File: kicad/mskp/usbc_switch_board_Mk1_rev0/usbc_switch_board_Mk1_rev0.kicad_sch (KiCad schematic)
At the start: 26 parts, among them J1 USB_C_Receptacle_USB2.0_14P, J2 USB_C_Receptacle_USB2.0_14P, J3 USB_A, J4 Conn_01x04_Socket, J5 Conn_01x02_Socket, Q1 2N3904, Q2 2N3906, U1 FSUSB42MUX, U2 AMS1117-3.3, U3 AMS1117-2.5

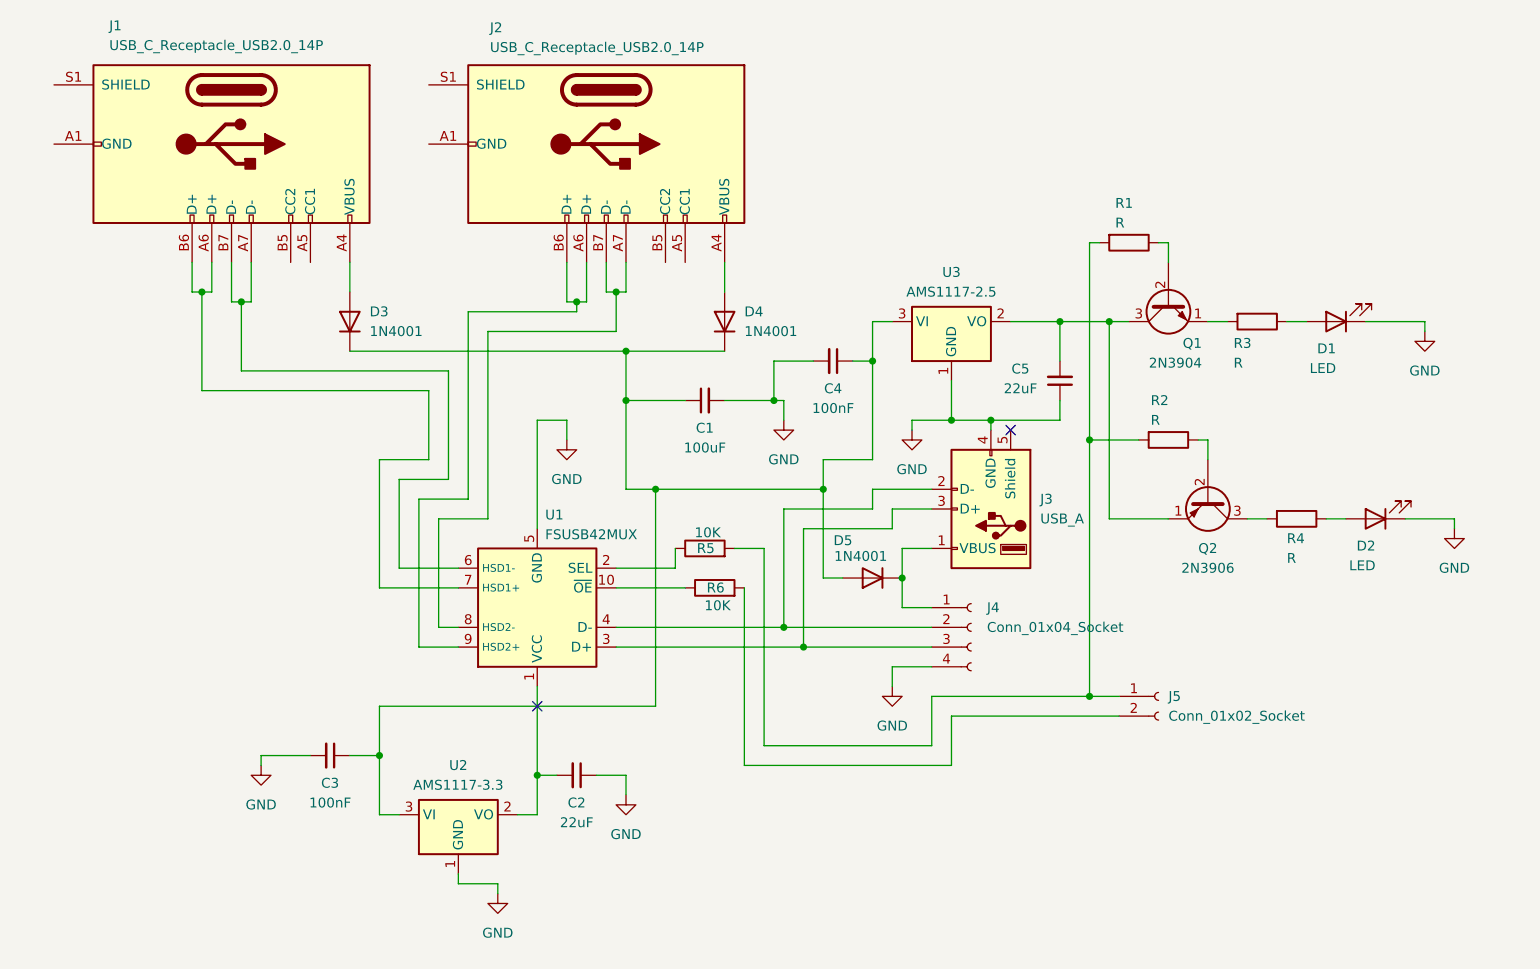
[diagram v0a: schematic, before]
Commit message: Remove unused ctrl mk1r1 in favor of mk2 first draft schematic
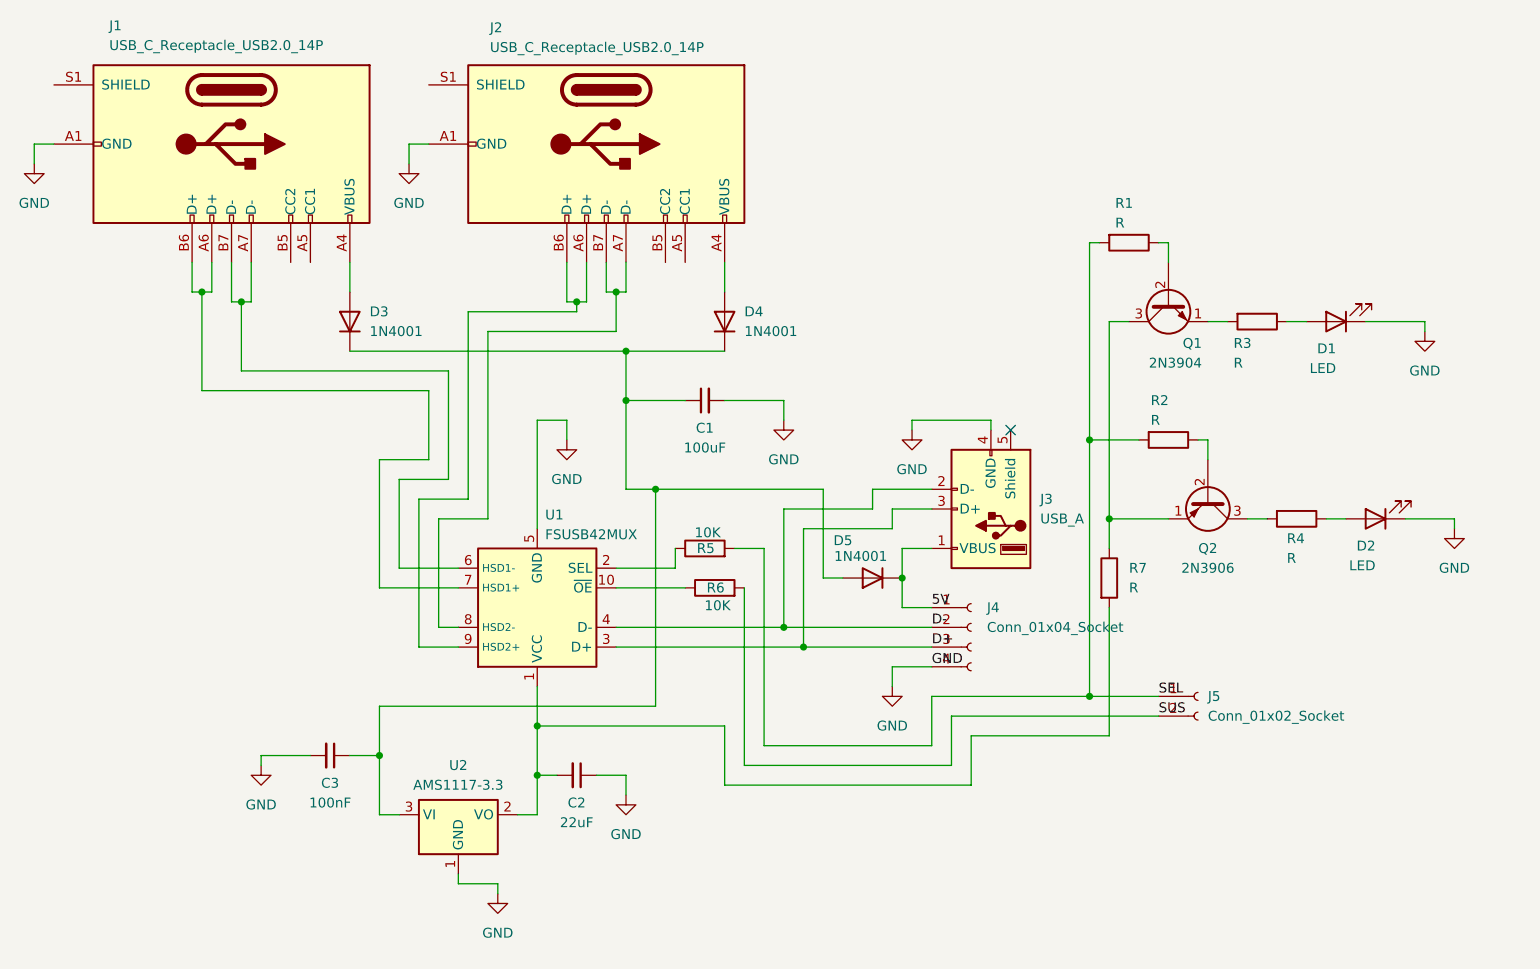
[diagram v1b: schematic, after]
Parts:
- removed C4: 100nF, symbol Device:C_Small
- removed C5: 22uF, symbol Device:C_Small
- removed U3: AMS1117-2.5, Package_TO_SOT_SMD:SOT-223-3_TabPin2, symbol Regulator_Linear:AMS1117-2.5
- added R7: R, symbol Device:R
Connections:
- net GND: now also J1.A1 (GND), J1.A12 (GND), J1.B1 (GND), J1.B12 (GND), J2.A1 (GND), J2.A12 (GND), J2.B1 (GND), J2.B12 (GND)
- net SEL: now reaches J5.1 (Pin_1), R1.2, R2.2, R5.2
- net SUS: now reaches J5.2 (Pin_2), R6.2
- net at C2.2, U1.1 (VCC), U2.2 (VO): now also R7.2
- net D+: now reaches J3.3 (D+), J4.3 (Pin_3), U1.3 (D+)
- net D-: now reaches J3.2 (D-), J4.2 (Pin_2), U1.4 (D-)
- net at Q1.3 (C), Q2.1 (E): now also R7.1
- net 5V: now reaches D5.1 (K), J3.1 (VBUS), J4.1 (Pin_1)
- no-connect marks 2 -> 1
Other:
- moved on the sheet: J5

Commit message: Adds first drafts of adc mouse and io expander mk2
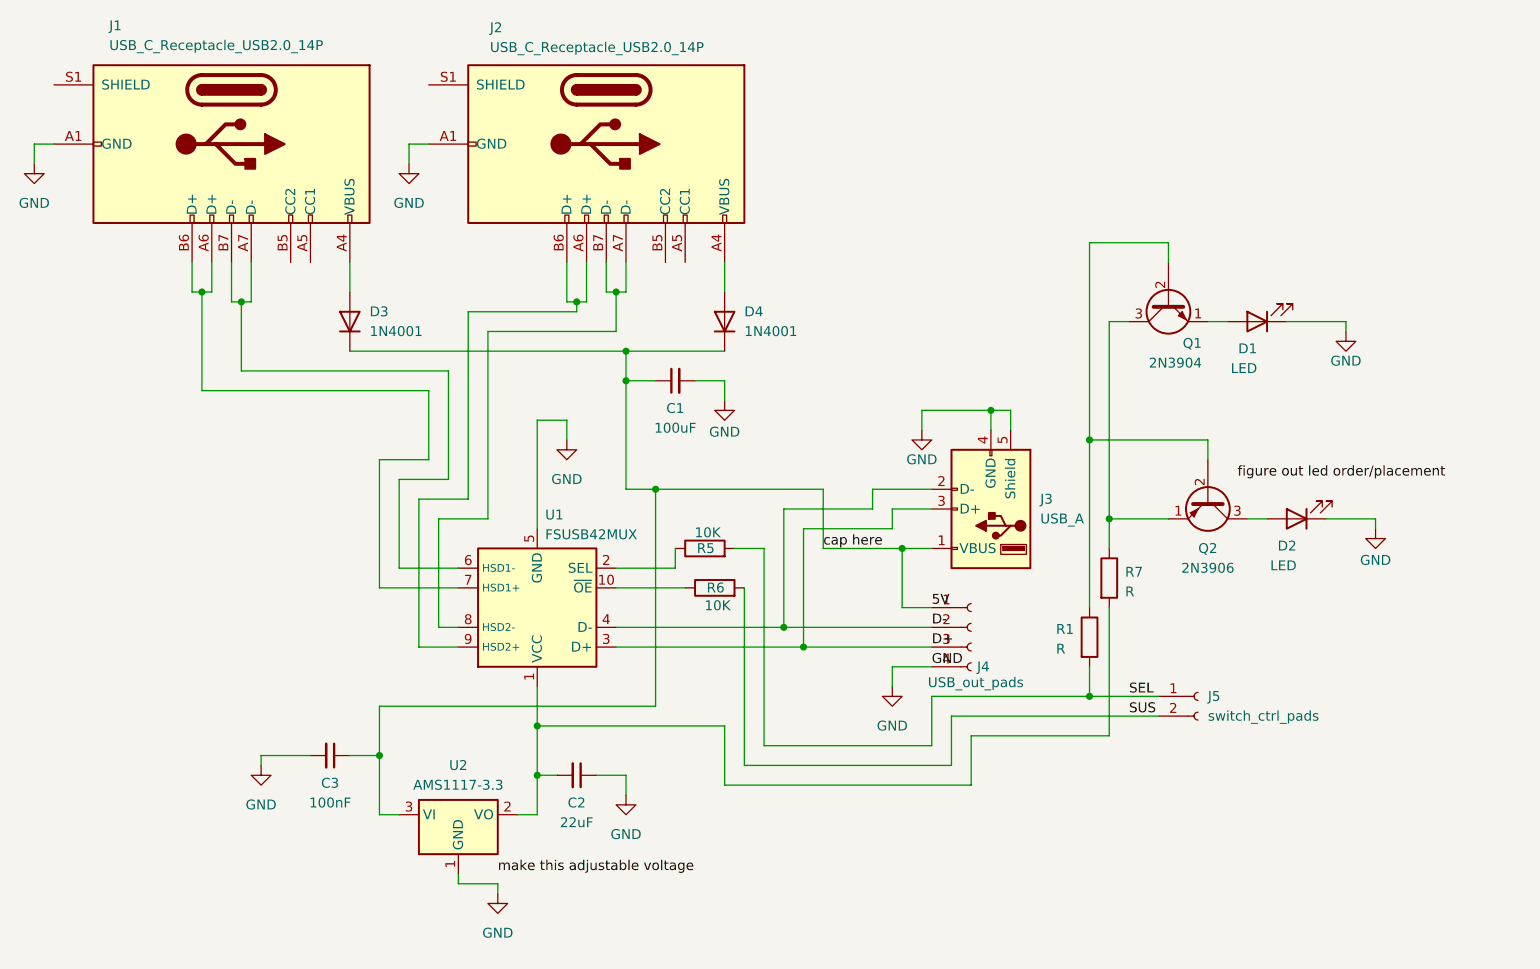
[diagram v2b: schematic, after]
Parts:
- removed D5: 1N4001, Diode_THT:D_DO-41_SOD81_P10.16mm_Horizontal, symbol Diode:1N4001
- removed R2, R3, R4: R, symbol Device:R
- J4: value Conn_01x04_Socket -> USB_out_pads
- J5: value Conn_01x02_Socket -> switch_ctrl_pads
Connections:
- net 5V: now also C1.1, C3.1, D3.1 (K), D4.1 (K), U2.3 (VI)
- net GND: now also J3.5 (Shield)
- net at D1.2 (A): now also Q1.1 (E)
- net at Q1.2 (B), R1.1: now also Q2.2 (B)
- net at D2.2 (A): now also Q2.3 (C)
- no-connect marks 1 -> 0
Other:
- moved on the sheet: C1, D1, D2

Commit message: Further refinement of first drafts adding specific components
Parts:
- added C4: C, symbol Device:C
- added R2, R3: VAR-R, symbol Device:R
- renumbered Q2 to Q1, Q1 to Q2
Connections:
- net 5V: now also C4.1
- net GND: now also J1.S1 (SHIELD), J2.S1 (SHIELD), C4.2, R3.1; no longer U2.1 (GND)
- net at D1.2 (A): now also Q1.3 (C); no longer Q2.1 (E)
- net at C2.2, R7.2, U1.1 (VCC)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: now also R2.2
- net at D2.2 (A): now also Q2.1 (E); no longer Q1.3 (C)
- new net: R2.1, R3.2, U2.1 (GND)
- no-connect marks 0 -> 4
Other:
- moved on the sheet: C1, C3, Q1, Q2, R5

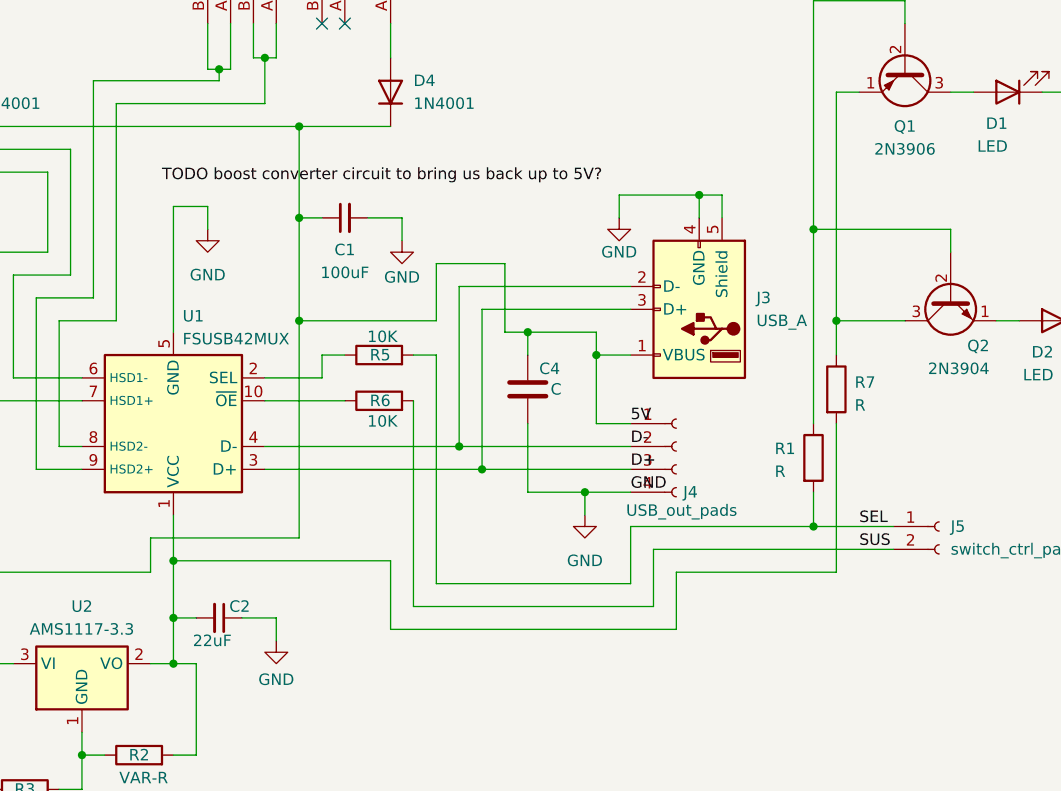
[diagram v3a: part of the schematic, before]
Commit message: Initital footprint assignment to all control boards
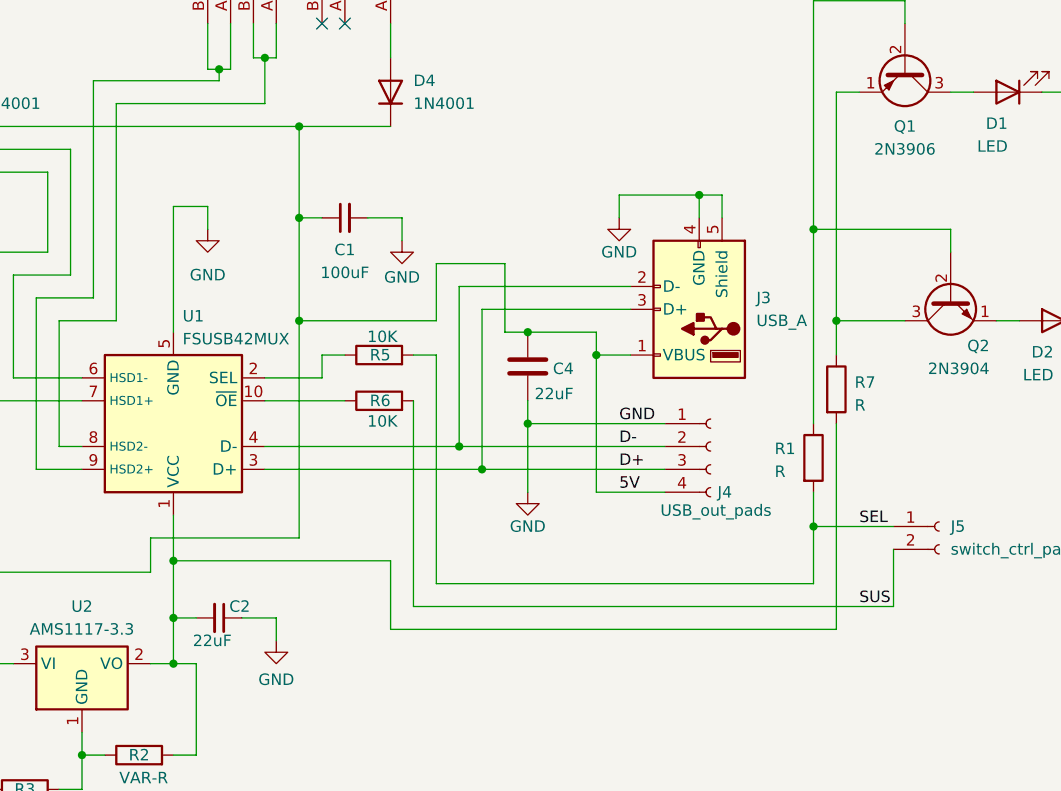
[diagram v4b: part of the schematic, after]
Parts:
- C1, C2, C3: footprint (none) -> Capacitor_SMD:C_1206_3216Metric_Pad1.33x1.80mm_HandSolder
- C4: value C -> 22uF; footprint (none) -> Capacitor_SMD:C_1206_3216Metric_Pad1.33x1.80mm_HandSolder
- D1, D2: footprint (none) -> LED_SMD:LED_0805_2012Metric_Pad1.15x1.40mm_HandSolder
- J1, J2: footprint (none) -> Connector_USB:USB_C_Receptacle_GCT_USB4110
- J3: footprint (none) -> Connector_USB:USB_A_CONNFLY_DS1095-WNR0
- J4: footprint (none) -> Connector_PinHeader_2.54mm:PinHeader_1x04_P2.54mm_Vertical
- J5: footprint (none) -> Connector_PinHeader_2.54mm:PinHeader_1x02_P2.54mm_Vertical
- R1, R2, R3, R5, R6, R7: footprint (none) -> Resistor_THT:R_Axial_DIN0207_L6.3mm_D2.5mm_P7.62mm_Horizontal
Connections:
- net 5V: now also J4.4 (Pin_4); no longer J4.1 (Pin_1)
- net GND: now also J4.1 (Pin_1); no longer J4.4 (Pin_4)
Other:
- moved on the sheet: C4, J4

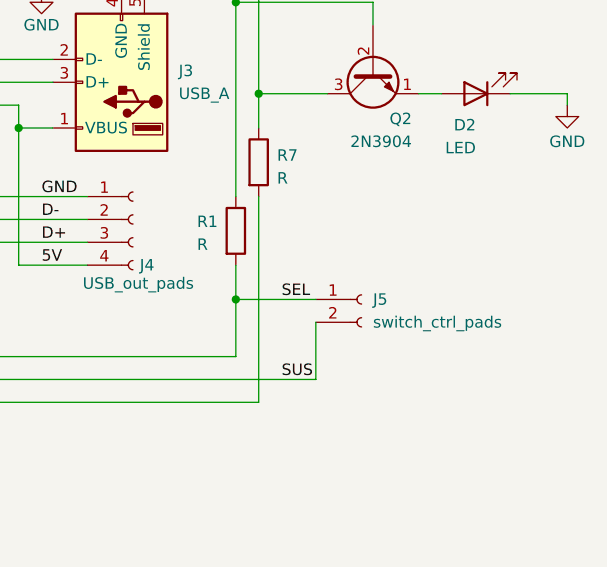
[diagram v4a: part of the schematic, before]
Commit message: Refining PCB outlines for pico and io control boards
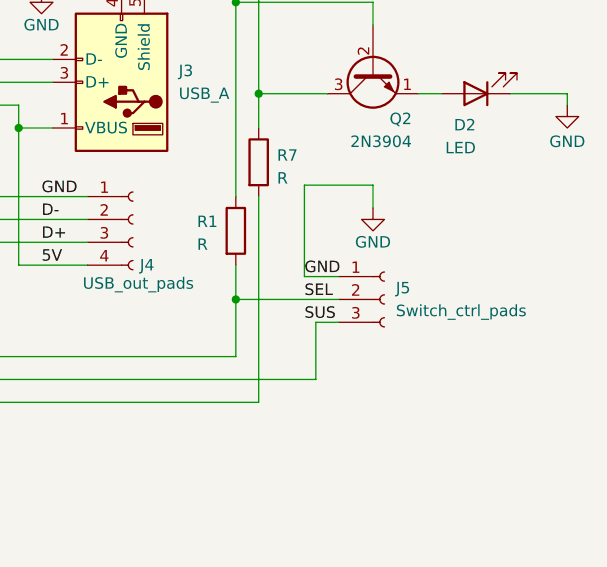
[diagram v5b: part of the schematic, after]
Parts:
- removed J5: switch_ctrl_pads, Connector_PinHeader_2.54mm:PinHeader_1x02_P2.54mm_Vertical, symbol Connector:Conn_01x02_Socket
- added J5: Switch_ctrl_pads, Connector_PinSocket_2.54mm:PinSocket_1x03_P2.54mm_Vertical, symbol Connector:Conn_01x03_Socket
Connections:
- net GND: now also J5.1 (Pin_1)
- net SEL: now also J5.2 (Pin_2)
- net SUS: no longer R6.2
- new net: J5.3 (Pin_3), R6.2
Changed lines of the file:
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@@
+	(wire
+		(pts
+			(xy 194.31 104.14) (xy 194.31 106.68)
+		)
+		(stroke
+			(width 0)
+			(type default)
+		)
+	)
 	(wire
 		(pts
@@
 	(wire
 		(pts
+			(xy 186.69 114.3) (xy 190.5 114.3)
+		)
+		(stroke
+			(width 0)
+			(type default)
+		)
+	)
+	(wire
+		(pts
 			(xy 124.46 97.79) (xy 124.46 100.33)
 		)
@@
 	(wire
 		(pts
+			(xy 187.96 119.38) (xy 190.5 119.38)
+		)
+		(stroke
+			(width 0)
+			(type default)
+		)
+	)
+	(wire
+		(pts
 			(xy 107.95 81.28) (xy 111.76 81.28)
 		)
@@
 	(wire
 		(pts
+			(xy 186.69 104.14) (xy 194.31 104.14)
+		)
+		(stroke
+			(width 0)
+			(type default)
+		)
+	)
+	(wire
+		(pts
 			(xy 68.58 60.96) (xy 68.58 66.04)
 		)
@@
 	(wire
 		(pts
+			(xy 186.69 104.14) (xy 186.69 114.3)
+		)
+		(stroke
+			(width 0)
+			(type default)
+		)
+	)
+	(wire
+		(pts
 			(xy 118.11 107.95) (xy 139.7 107.95)
 		)
@@
 	(wire
 		(pts
-			(xy 179.07 116.84) (xy 187.96 116.84)
+			(xy 179.07 116.84) (xy 190.5 116.84)
 		)
 		(stroke
@@
 	)
 	(label "SUS"
-		(at 184.15 125.73 0)
+		(at 186.69 119.38 0)
 		(fields_autoplaced yes)
 		(effects
@@
 	)
 	(label "SEL"
-		(at 184.15 116.84 0)
+		(at 186.69 116.84 0)
+		(fields_autoplaced yes)
+		(effects
+			(font
+				(size 1.27 1.27)
+			)
+			(justify left bottom)
+		)
+	)
+	(label "GND"
+		(at 186.69 114.3 0)
 		(fields_autoplaced yes)
 		(effects
@@
 			)
 			(justify left bottom)
+		)
+	)
+	(symbol
+		(lib_id "Connector:Conn_01x03_Socket")
+		(at 195.58 116.84 0)
+		(unit 1)
+		(exclude_from_sim no)
+		(in_bom yes)
+		(on_board yes)
+		(dnp no)
+		(fields_autoplaced yes)
+		(property "Reference" "J5"
+			(at 196.85 115.5699 0)
+			(effects
+				(font
+					(size 1.27 1.27)
+				)
+				(justify left)
+			)
+		)
+		(property "Value" "Switch_ctrl_pads"
+			(at 196.85 118.1099 0)
+			(effects
+				(font
+					(size 1.27 1.27)
+				)
+				(justify left)
+			)
+		)
+		(property "Footprint" "Connector_PinSocket_2.54mm:PinSocket_1x03_P2.54mm_Vertical"
+			(at 195.58 116.84 0)
+			(effects
+				(font
+					(size 1.27 1.27)
+				)
+				(hide yes)
+			)
+		)
+		(property "Datasheet" "~"
+			(at 195.58 116.84 0)
+			(effects
+				(font
+					(size 1.27 1.27)
+				)
+				(hide yes)
+			)
+		)
+		(property "Description" "Generic connector, single row, 01x03, script generated"
+			(at 195.58 116.84 0)
+			(effects
+				(font
+					(size 1.27 1.27)
+				)
+				(hide yes)
+			)
+		)
+		(pin "1"
+		)
+		(pin "3"
+		)
+		(pin "2"
+		)
+		(instances
+			(project "usbc_switch_board_Mk1_rev0"
+				(path "/0657c12e-f5d6-4d04-bbd3-655b6c3f3660"
+					(reference "J5")
+					(unit 1)
+				)
+			)
 		)
 	)
@@
 				(path "/0657c12e-f5d6-4d04-bbd3-655b6c3f3660"
 					(reference "R3")
+					(unit 1)
+				)
+			)
+		)
+	)
+	(symbol
+		(lib_id "power:GND")
+		(at 194.31 106.68 0)
+		(unit 1)
+		(exclude_from_sim no)
+		(in_bom yes)
+		(on_board yes)
+		(dnp no)
+		(property "Reference" "#PWR03"
+			(at 194.31 113.03 0)
+			(effects
+				(font
+					(size 1.27 1.27)
+				)
+				(hide yes)
+			)
+		)
+		(property "Value" "GND"
+			(at 194.31 110.49 0)
+			(effects
+				(font
+					(size 1.27 1.27)
+				)
+			)
+		)
+		(property "Footprint" ""
+			(at 194.31 106.68 0)
+			(effects
+				(font
+					(size 1.27 1.27)
+				)
+				(hide yes)
+			)
+		)
+		(property "Datasheet" ""
+			(at 194.31 106.68 0)
+			(effects
+				(font
+					(size 1.27 1.27)
+				)
+				(hide yes)
+			)
+		)
+		(property "Description" "Power symbol creates a global label with name \"GND\" , ground"
+			(at 194.31 106.68 0)
+			(effects
+				(font
+					(size 1.27 1.27)
+				)
+				(hide yes)
+			)
+		)
+		(pin "1"
+		)
+		(instances
+			(project "usbc_switch_board_Mk1_rev0"
+				(path "/0657c12e-f5d6-4d04-bbd3-655b6c3f3660"
+					(reference "#PWR03")
 					(unit 1)
 				)
@@
 					(unit 1)
 				)
-			)
-		)
-	)
-	(symbol
-		(lib_id "Connector:Conn_01x02_Socket")
-		(at 193.04 116.84 0)
-		(unit 1)
-		(exclude_from_sim no)
-		(in_bom yes)
-		(on_board yes)
-		(dnp no)
-		(fields_autoplaced yes)
-		(property "Reference" "J5"
-			(at 194.31 116.8399 0)
-			(effects
-				(font
-					(size 1.27 1.27)
-				)
-				(justify left)
-			)
-		)
-		(property "Value" "switch_ctrl_pads"
-			(at 194.31 119.3799 0)
-			(effects
-				(font
-					(size 1.27 1.27)
-				)
-				(justify left)
-			)
-		)
-		(property "Footprint" "Connector_PinHeader_2.54mm:PinHeader_1x02_P2.54mm_Vertical"
-			(at 193.04 116.84 0)
-			(effects
-				(font
-					(size 1.27 1.27)
-				)
-				(hide yes)
-			)
-		)
-		(property "Datasheet" "~"
-			(at 193.04 116.84 0)
-			(effects
-				(font
-					(size 1.27 1.27)
-				)
-				(hide yes)
-			)
-		)
-		(property "Description" "Generic connector, single row, 01x02, script generated"
-			(at 193.04 116.84 0)
-			(effects
-				(font
-					(size 1.27 1.27)
-				)
-				(hide yes)
-			)
-		)
-		(pin "1"
-		)
-		(pin "2"
-		)
-		(instances
-			(project "usbc_switch_board_Mk1_rev0"
-				(path "/0657c12e-f5d6-4d04-bbd3-655b6c3f3660"
-					(reference "J5")
-					(unit 1)
-				)
